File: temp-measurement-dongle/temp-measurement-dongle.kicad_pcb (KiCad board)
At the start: 2 copper layers, 70.3 x 67.5 mm, 73 parts, among them J1 USB2UART, J2 1.47 IPS LCD, J3 ConnBattery, J4 RTD_PT100, Q1 SS8050, Q2 SS8050, Q3 SS8050, SW1 RST, SW2 IN1, SW3 Boot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

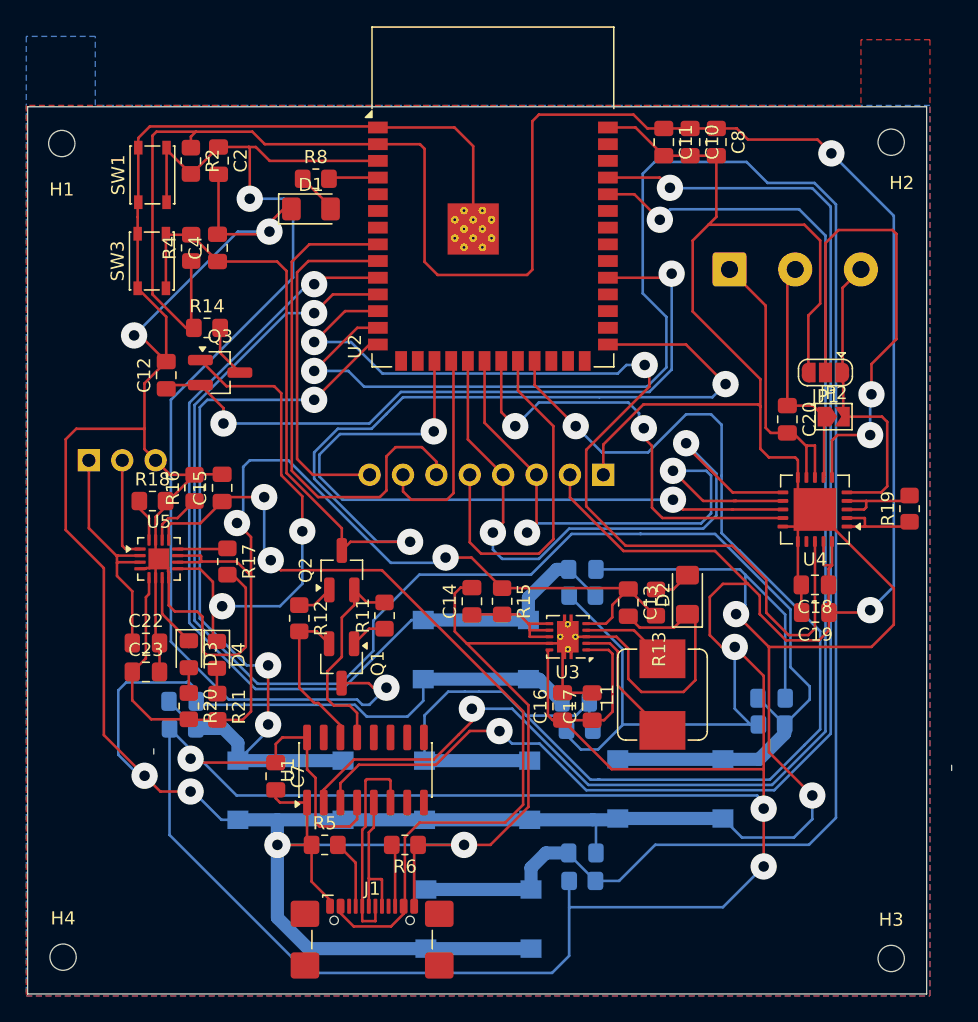
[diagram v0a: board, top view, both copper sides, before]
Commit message: feat: update route, flipped lcd screen
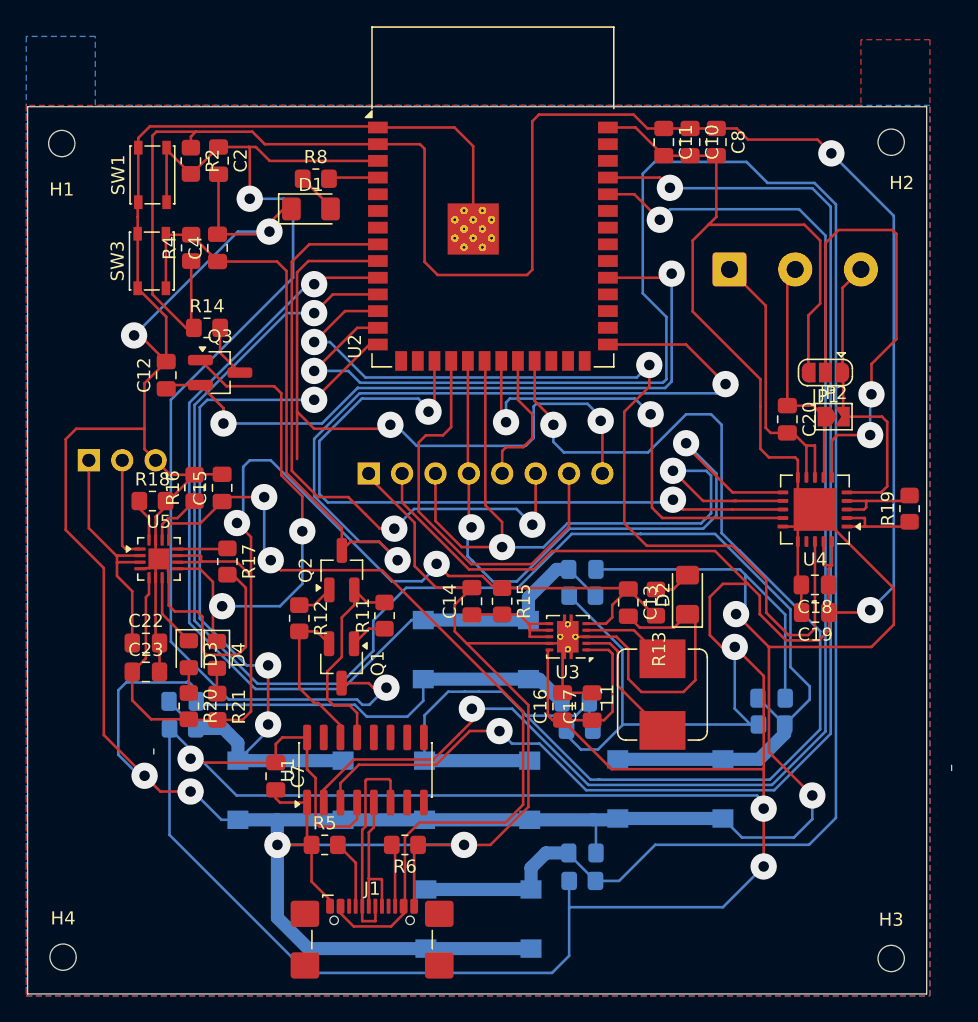
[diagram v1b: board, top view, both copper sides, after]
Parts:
- moved J2 17.9 mm to (127.5, 95.5), turned to -90 degrees
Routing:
- net /BLK: track 26.7 -> 52.6 mm, vias 0 -> 2
- net /RESET: track 27.0 -> 10.7 mm
- net /CS: track 15.7 -> 31.8 mm
- net +3.3V: track 404.6 -> 418.8 mm
- net /SCK: track 45.0 -> 56.6 mm
- net /DC: track 39.4 -> 48.2 mm, vias 0 -> 2
- net /MAX31865DRDY: track 74.9 -> 72.0 mm
- net /MOSI: track 49.9 -> 52.7 mm
- net GND: track 547.2 -> 544.6 mm
- net /IN5: track 100.2 -> 101.9 mm
- net /MISO: track 33.8 -> 35.4 mm
- net /MAX31865CS: track 52.8 -> 54.2 mm
- net VDD: track 88.9 -> 89.8 mm
- net /IO0: track 97.9 -> 98.6 mm
- net Net-(Q3-E): track 54.4 -> 55.0 mm
